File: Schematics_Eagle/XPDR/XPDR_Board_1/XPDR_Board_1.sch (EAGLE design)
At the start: 40 parts

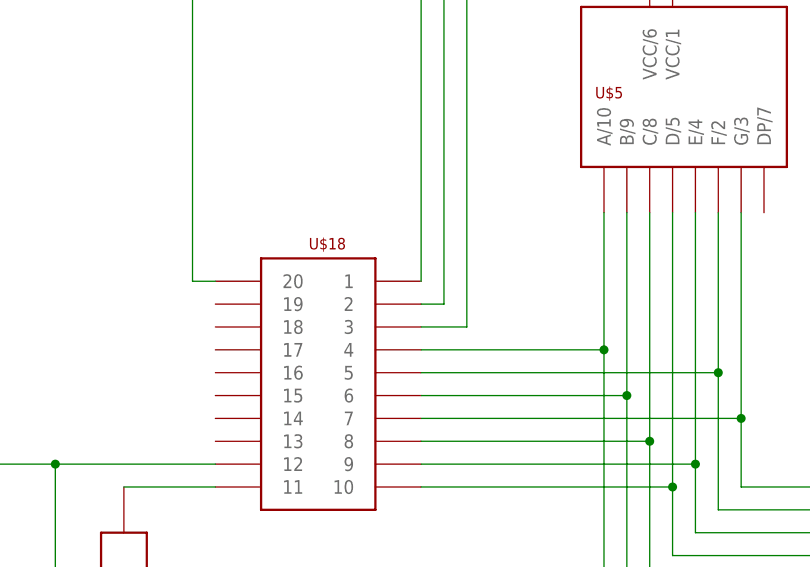
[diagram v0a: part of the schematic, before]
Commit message: Both XPDR boards finished.
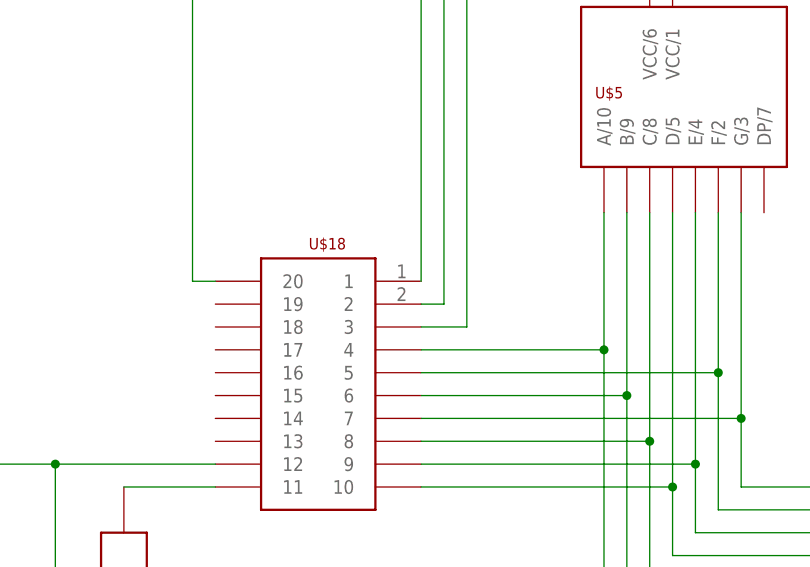
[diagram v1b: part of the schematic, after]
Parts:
- U$1, U$2, U$3, U$4: device RadioStack_v2:PEC11R -> library:PEC11R
- U$10: device RadioStack_v2:LED_5MM -> library:LED_5MM
- U$11, U$12, U$13, U$14, U$15, U$16, U$19, U$20, U$21, U$22, U$23, U$24, U$25, U$26, U$27, U$28, U$30, U$31, U$40: device RadioStack_v2:REZISTOR -> library:REZISTOR
- U$17: device RadioStack_v2:LISTA_2X5 -> library:LISTA_2X5
- U$18: device RadioStack_v2:LISTA_2X10 -> library:LISTA_2X10
- U$29, U$32, U$33, U$35, U$36, U$37: device RadioStack_v2:KONDENZATOR_SIROKY -> library:KONDENZATOR_SIROKY
- U$34, U$38, U$39: device RadioStack_v2:KONDENZATOR -> library:KONDENZATOR
- U$5, U$6, U$7, U$8: device RadioStack_v2:SA3611EWA -> library:SA3611EWA
- U$9: device RadioStack_v2:P1-0S -> library:P1-0S
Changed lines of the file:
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@@
 </classes>
 <parts>
-<part name="U$1" library="RadioStack_v2" deviceset="PEC11R" device=""/>
-<part name="U$2" library="RadioStack_v2" deviceset="PEC11R" device=""/>
-<part name="U$3" library="RadioStack_v2" deviceset="PEC11R" device=""/>
-<part name="U$4" library="RadioStack_v2" deviceset="PEC11R" device=""/>
-<part name="U$5" library="RadioStack_v2" deviceset="SA3611EWA" device=""/>
-<part name="U$6" library="RadioStack_v2" deviceset="SA3611EWA" device=""/>
-<part name="U$7" library="RadioStack_v2" deviceset="SA3611EWA" device=""/>
-<part name="U$8" library="RadioStack_v2" deviceset="SA3611EWA" device=""/>
-<part name="U$9" library="RadioStack_v2" deviceset="P1-0S" device=""/>
-<part name="U$10" library="RadioStack_v2" deviceset="LED_5MM" device=""/>
-<part name="U$17" library="RadioStack_v2" deviceset="LISTA_2X5" device=""/>
-<part name="U$18" library="RadioStack_v2" deviceset="LISTA_2X10" device=""/>
-<part name="U$11" library="RadioStack_v2" deviceset="REZISTOR" device="" value=""/>
-<part name="U$12" library="RadioStack_v2" deviceset="REZISTOR" device="" value=""/>
-<part name="U$13" library="RadioStack_v2" deviceset="REZISTOR" device="" value=""/>
-<part name="U$14" library="RadioStack_v2" deviceset="REZISTOR" device="" value=""/>
-<part name="U$15" library="RadioStack_v2" deviceset="REZISTOR" device="" value=""/>
-<part name="U$16" library="RadioStack_v2" deviceset="REZISTOR" device="" value=""/>
-<part name="U$19" library="RadioStack_v2" deviceset="REZISTOR" device="" value=""/>
-<part name="U$20" library="RadioStack_v2" deviceset="REZISTOR" device="" value=""/>
-<part name="U$21" library="RadioStack_v2" deviceset="REZISTOR" device="" value=""/>
-<part name="U$22" library="RadioStack_v2" deviceset="REZISTOR" device="" value=""/>
-<part name="U$23" library="RadioStack_v2" deviceset="REZISTOR" device="" value=""/>
-<part name="U$24" library="RadioStack_v2" deviceset="REZISTOR" device="" value=""/>
-<part name="U$25" library="RadioStack_v2" deviceset="REZISTOR" device="" value=""/>
-<part name="U$26" library="RadioStack_v2" deviceset="REZISTOR" device="" value=""/>
-<part name="U$27" library="RadioStack_v2" deviceset="REZISTOR" device="" value=""/>
-<part name="U$28" library="RadioStack_v2" deviceset="REZISTOR" device="" value=""/>
-<part name="U$30" library="RadioStack_v2" deviceset="REZISTOR" device="" value=""/>
-<part name="U$31" library="RadioStack_v2" deviceset="REZISTOR" device="" value=""/>
-<part name="U$29" library="RadioStack_v2" deviceset="KONDENZATOR_SIROKY" device=""/>
-<part name="U$32" library="RadioStack_v2" deviceset="KONDENZATOR_SIROKY" device=""/>
-<part name="U$33" library="RadioStack_v2" deviceset="KONDENZATOR_SIROKY" device=""/>
-<part name="U$34" library="RadioStack_v2" deviceset="KONDENZATOR" device=""/>
-<part name="U$35" library="RadioStack_v2" deviceset="KONDENZATOR_SIROKY" device=""/>
-<part name="U$36" library="RadioStack_v2" deviceset="KONDENZATOR_SIROKY" device=""/>
-<part name="U$37" library="RadioStack_v2" deviceset="KONDENZATOR_SIROKY" device=""/>
-<part name="U$38" library="RadioStack_v2" deviceset="KONDENZATOR" device=""/>
-<part name="U$39" library="RadioStack_v2" deviceset="KONDENZATOR" device=""/>
-<part name="U$40" library="RadioStack_v2" deviceset="REZISTOR" device="" value=""/>
+<part name="U$1" library="library" deviceset="PEC11R" device=""/>
+<part name="U$2" library="library" deviceset="PEC11R" device=""/>
+<part name="U$3" library="library" deviceset="PEC11R" device=""/>
+<part name="U$4" library="library" deviceset="PEC11R" device=""/>
+<part name="U$5" library="library" deviceset="SA3611EWA" device=""/>
+<part name="U$6" library="library" deviceset="SA3611EWA" device=""/>
+<part name="U$7" library="library" deviceset="SA3611EWA" device=""/>
+<part name="U$8" library="library" deviceset="SA3611EWA" device=""/>
+<part name="U$9" library="library" deviceset="P1-0S" device=""/>
+<part name="U$10" library="library" deviceset="LED_5MM" device=""/>
+<part name="U$17" library="library" deviceset="LISTA_2X5" device=""/>
+<part name="U$18" library="library" deviceset="LISTA_2X10" device=""/>
+<part name="U$11" library="library" deviceset="REZISTOR" device="" value="REZISTOR"/>
+<part name="U$12" library="library" deviceset="REZISTOR" device="" value="REZISTOR"/>
+<part name="U$13" library="library" deviceset="REZISTOR" device="" value="REZISTOR"/>
+<part name="U$14" library="library" deviceset="REZISTOR" device="" value="REZISTOR"/>
+<part name="U$15" library="library" deviceset="REZISTOR" device="" value="REZISTOR"/>
+<part name="U$16" library="library" deviceset="REZISTOR" device="" value="REZISTOR"/>
+<part name="U$19" library="library" deviceset="REZISTOR" device="" value="REZISTOR"/>
+<part name="U$20" library="library" deviceset="REZISTOR" device="" value="REZISTOR"/>
+<part name="U$21" library="library" deviceset="REZISTOR" device="" value="REZISTOR"/>
+<part name="U$22" library="library" deviceset="REZISTOR" device="" value="REZISTOR"/>
+<part name="U$23" library="library" deviceset="REZISTOR" device="" value="REZISTOR"/>
+<part name="U$24" library="library" deviceset="REZISTOR" device="" value="REZISTOR"/>
+<part name="U$25" library="library" deviceset="REZISTOR" device="" value="REZISTOR"/>
+<part name="U$26" library="library" deviceset="REZISTOR" device="" value="REZISTOR"/>
+<part name="U$27" library="library" deviceset="REZISTOR" device="" value="REZISTOR"/>
+<part name="U$28" library="library" deviceset="REZISTOR" device="" value="REZISTOR"/>
+<part name="U$30" library="library" deviceset="REZISTOR" device="" value="REZISTOR"/>
+<part name="U$31" library="library" deviceset="REZISTOR" device="" value="REZISTOR"/>
+<part name="U$29" library="library" deviceset="KONDENZATOR_SIROKY" device=""/>
+<part name="U$32" library="library" deviceset="KONDENZATOR_SIROKY" device=""/>
+<part name="U$33" library="library" deviceset="KONDENZATOR_SIROKY" device=""/>
+<part name="U$34" library="library" deviceset="KONDENZATOR" device=""/>
+<part name="U$35" library="library" deviceset="KONDENZATOR_SIROKY" device=""/>
+<part name="U$36" library="library" deviceset="KONDENZATOR_SIROKY" device=""/>
+<part name="U$37" library="library" deviceset="KONDENZATOR_SIROKY" device=""/>
+<part name="U$38" library="library" deviceset="KONDENZATOR" device=""/>
+<part name="U$39" library="library" deviceset="KONDENZATOR" device=""/>
+<part name="U$40" library="library" deviceset="REZISTOR" device="" value="REZISTOR"/>
 </parts>
 <sheets>
